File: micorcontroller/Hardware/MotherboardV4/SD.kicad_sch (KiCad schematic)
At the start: 11 parts, among them J1 693072010801

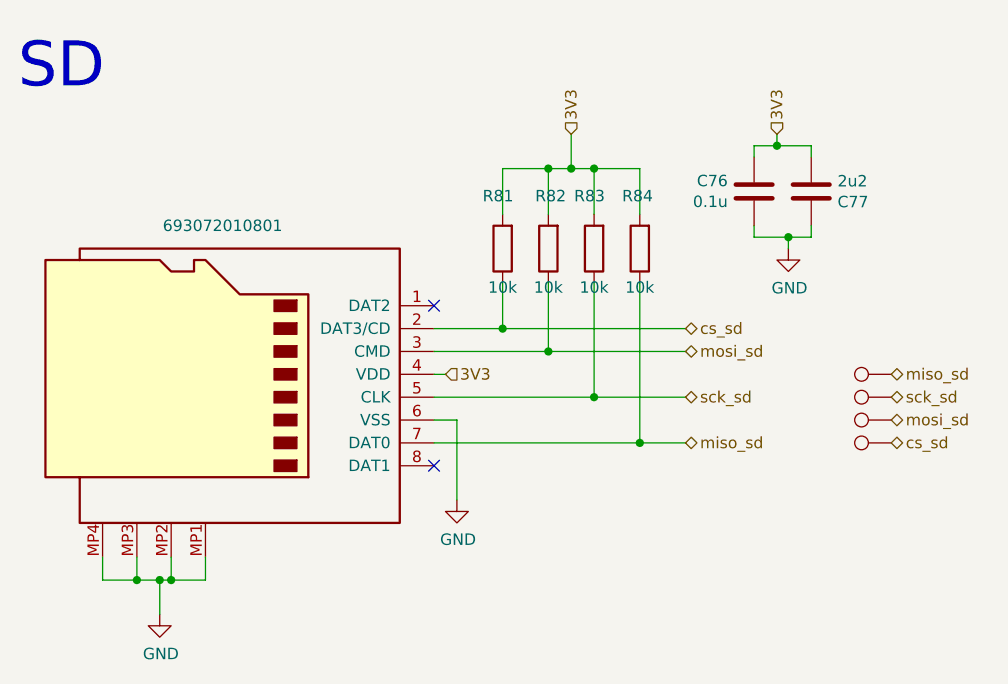
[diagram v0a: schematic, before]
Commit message: added NTC calculation
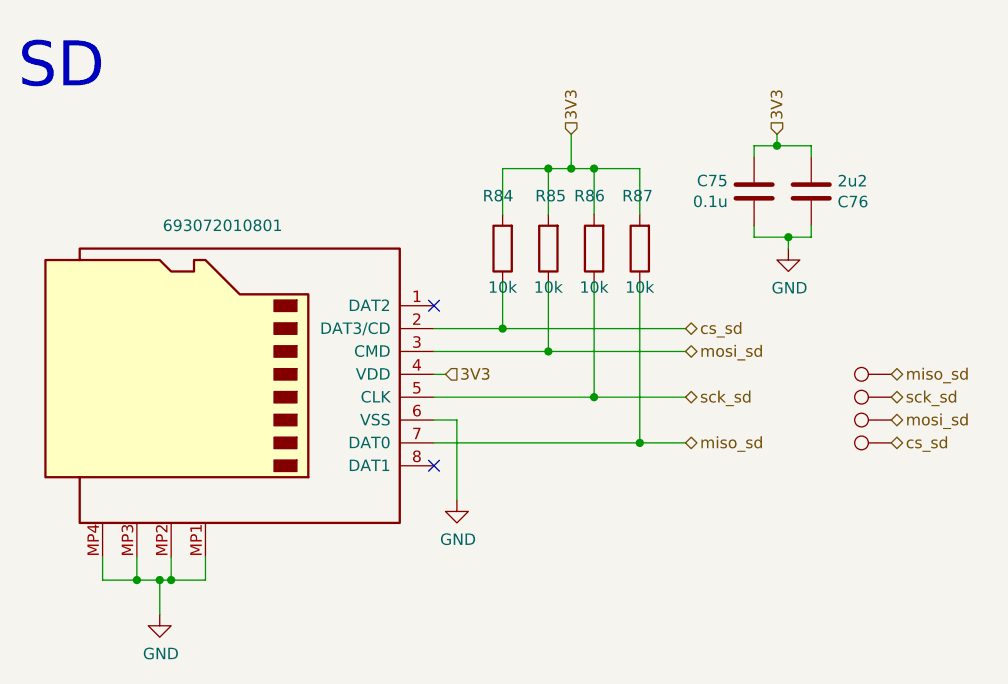
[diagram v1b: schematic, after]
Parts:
- renumbered C76 to C75, C77 to C76, J1 to J4, R81 to R84, R82 to R85, R83 to R86, R84 to R87, TP2 to TP6, TP3 to TP7, TP4 to TP8, TP5 to TP9
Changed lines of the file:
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@@
 		(on_board yes)
 		(dnp no)
-		(property "Reference" "TP4"
+		(property "Reference" "TP8"
 			(at 111.125 60.96 90)
 			(effects
@@
 			(project "BalloonMotherboardV4"
 				(path "/a70d325c-f83f-4714-a2b6-4ef8919d016e/a8132881-ef2f-4675-97ba-225bfc38fe3d"
-					(reference "TP4")
+					(reference "TP8")
 					(unit 1)
 				)
@@
 		(on_board yes)
 		(dnp no)
-		(property "Reference" "R84"
+		(property "Reference" "R87"
 			(at 88.646 34.798 0)
 			(effects
@@
 			(project "BalloonMotherboardV4"
 				(path "/a70d325c-f83f-4714-a2b6-4ef8919d016e/a8132881-ef2f-4675-97ba-225bfc38fe3d"
-					(reference "R84")
+					(reference "R87")
 					(unit 1)
 				)
@@
 		(on_board yes)
 		(dnp no)
-		(property "Reference" "TP2"
+		(property "Reference" "TP6"
 			(at 111.125 55.88 90)
 			(effects
@@
 			(project "BalloonMotherboardV4"
 				(path "/a70d325c-f83f-4714-a2b6-4ef8919d016e/a8132881-ef2f-4675-97ba-225bfc38fe3d"
-					(reference "TP2")
+					(reference "TP6")
 					(unit 1)
 				)
@@
 		(on_board yes)
 		(dnp no)
-		(property "Reference" "C77"
+		(property "Reference" "C76"
 			(at 110.871 35.4584 0)
 			(effects
@@
 			(project "BalloonMotherboardV4"
 				(path "/a70d325c-f83f-4714-a2b6-4ef8919d016e/a8132881-ef2f-4675-97ba-225bfc38fe3d"
-					(reference "C77")
+					(reference "C76")
 					(unit 1)
 				)
@@
 		(on_board yes)
 		(dnp no)
-		(property "Reference" "R81"
+		(property "Reference" "R84"
 			(at 73.152 34.798 0)
 			(effects
@@
 			(project "BalloonMotherboardV4"
 				(path "/a70d325c-f83f-4714-a2b6-4ef8919d016e/a8132881-ef2f-4675-97ba-225bfc38fe3d"
-					(reference "R81")
+					(reference "R84")
 					(unit 1)
 				)
@@
 		(on_board yes)
 		(dnp no)
-		(property "Reference" "TP3"
+		(property "Reference" "TP7"
 			(at 111.125 58.42 90)
 			(effects
@@
 			(project "BalloonMotherboardV4"
 				(path "/a70d325c-f83f-4714-a2b6-4ef8919d016e/a8132881-ef2f-4675-97ba-225bfc38fe3d"
-					(reference "TP3")
+					(reference "TP7")
 					(unit 1)
 				)
@@
 		(on_board yes)
 		(dnp no)
-		(property "Reference" "R82"
+		(property "Reference" "R85"
 			(at 78.994 34.798 0)
 			(effects
@@
 			(project "BalloonMotherboardV4"
 				(path "/a70d325c-f83f-4714-a2b6-4ef8919d016e/a8132881-ef2f-4675-97ba-225bfc38fe3d"
-					(reference "R82")
+					(reference "R85")
 					(unit 1)
 				)
@@
 		(on_board yes)
 		(dnp no)
-		(property "Reference" "C76"
+		(property "Reference" "C75"
 			(at 98.679 33.1216 0)
 			(effects
@@
 			(project "BalloonMotherboardV4"
 				(path "/a70d325c-f83f-4714-a2b6-4ef8919d016e/a8132881-ef2f-4675-97ba-225bfc38fe3d"
-					(reference "C76")
+					(reference "C75")
 					(unit 1)
 				)
@@
 		(on_board yes)
 		(dnp no)
-		(property "Reference" "J1"
+		(property "Reference" "J4"
 			(at 42.545 35.56 0)
 			(effects
@@
 			(project "BalloonMotherboardV4"
 				(path "/a70d325c-f83f-4714-a2b6-4ef8919d016e/a8132881-ef2f-4675-97ba-225bfc38fe3d"
-					(reference "J1")
+					(reference "J4")
 					(unit 1)
 				)
@@
 		(on_board yes)
 		(dnp no)
-		(property "Reference" "#PWR042"
+		(property "Reference" "#PWR0127"
 			(at 35.56 87.63 0)
 			(effects
@@
 			(project "BalloonMotherboardV4"
 				(path "/a70d325c-f83f-4714-a2b6-4ef8919d016e/a8132881-ef2f-4675-97ba-225bfc38fe3d"
-					(reference "#PWR042")
+					(reference "#PWR0127")
 					(unit 1)
 				)
@@
 		(on_board yes)
 		(dnp no)
-		(property "Reference" "TP5"
+		(property "Reference" "TP9"
 			(at 111.125 63.5 90)
 			(effects
@@
 			(project "BalloonMotherboardV4"
 				(path "/a70d325c-f83f-4714-a2b6-4ef8919d016e/a8132881-ef2f-4675-97ba-225bfc38fe3d"
-					(reference "TP5")
+					(reference "TP9")
 					(unit 1)
 				)
@@
 		(on_board yes)
 		(dnp no)
-		(property "Reference" "#PWR05"
+		(property "Reference" "#PWR0129"
 			(at 105.41 46.99 0)
 			(effects
@@
 			(project "BalloonMotherboardV4"
 				(path "/a70d325c-f83f-4714-a2b6-4ef8919d016e/a8132881-ef2f-4675-97ba-225bfc38fe3d"
-					(reference "#PWR05")
+					(reference "#PWR0129")
 					(unit 1)
 				)
@@
 		(on_board yes)
 		(dnp no)
-		(property "Reference" "#PWR0108"
+		(property "Reference" "#PWR0128"
 			(at 68.58 74.93 0)
 			(effects
@@
 			(project "BalloonMotherboardV4"
 				(path "/a70d325c-f83f-4714-a2b6-4ef8919d016e/a8132881-ef2f-4675-97ba-225bfc38fe3d"
-					(reference "#PWR0108")
+					(reference "#PWR0128")
 					(unit 1)
 				)
@@
 		(on_board yes)
 		(dnp no)
-		(property "Reference" "R83"
+		(property "Reference" "R86"
 			(at 83.312 34.798 0)
 			(effects
@@
 			(project "BalloonMotherboardV4"
 				(path "/a70d325c-f83f-4714-a2b6-4ef8919d016e/a8132881-ef2f-4675-97ba-225bfc38fe3d"
-					(reference "R83")
-					(unit 1)
-				)
+					(reference "R86")
+					(unit 1)
+				)
